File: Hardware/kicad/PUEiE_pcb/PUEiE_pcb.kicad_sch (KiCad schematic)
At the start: 7 parts, among them J1 Screw_Terminal_01x02, J3 USB_C_Receptacle_USB2.0_16P, U3 USBLC6-2SC6, U4 DRV8461SPWP, U6 LIS3MDL

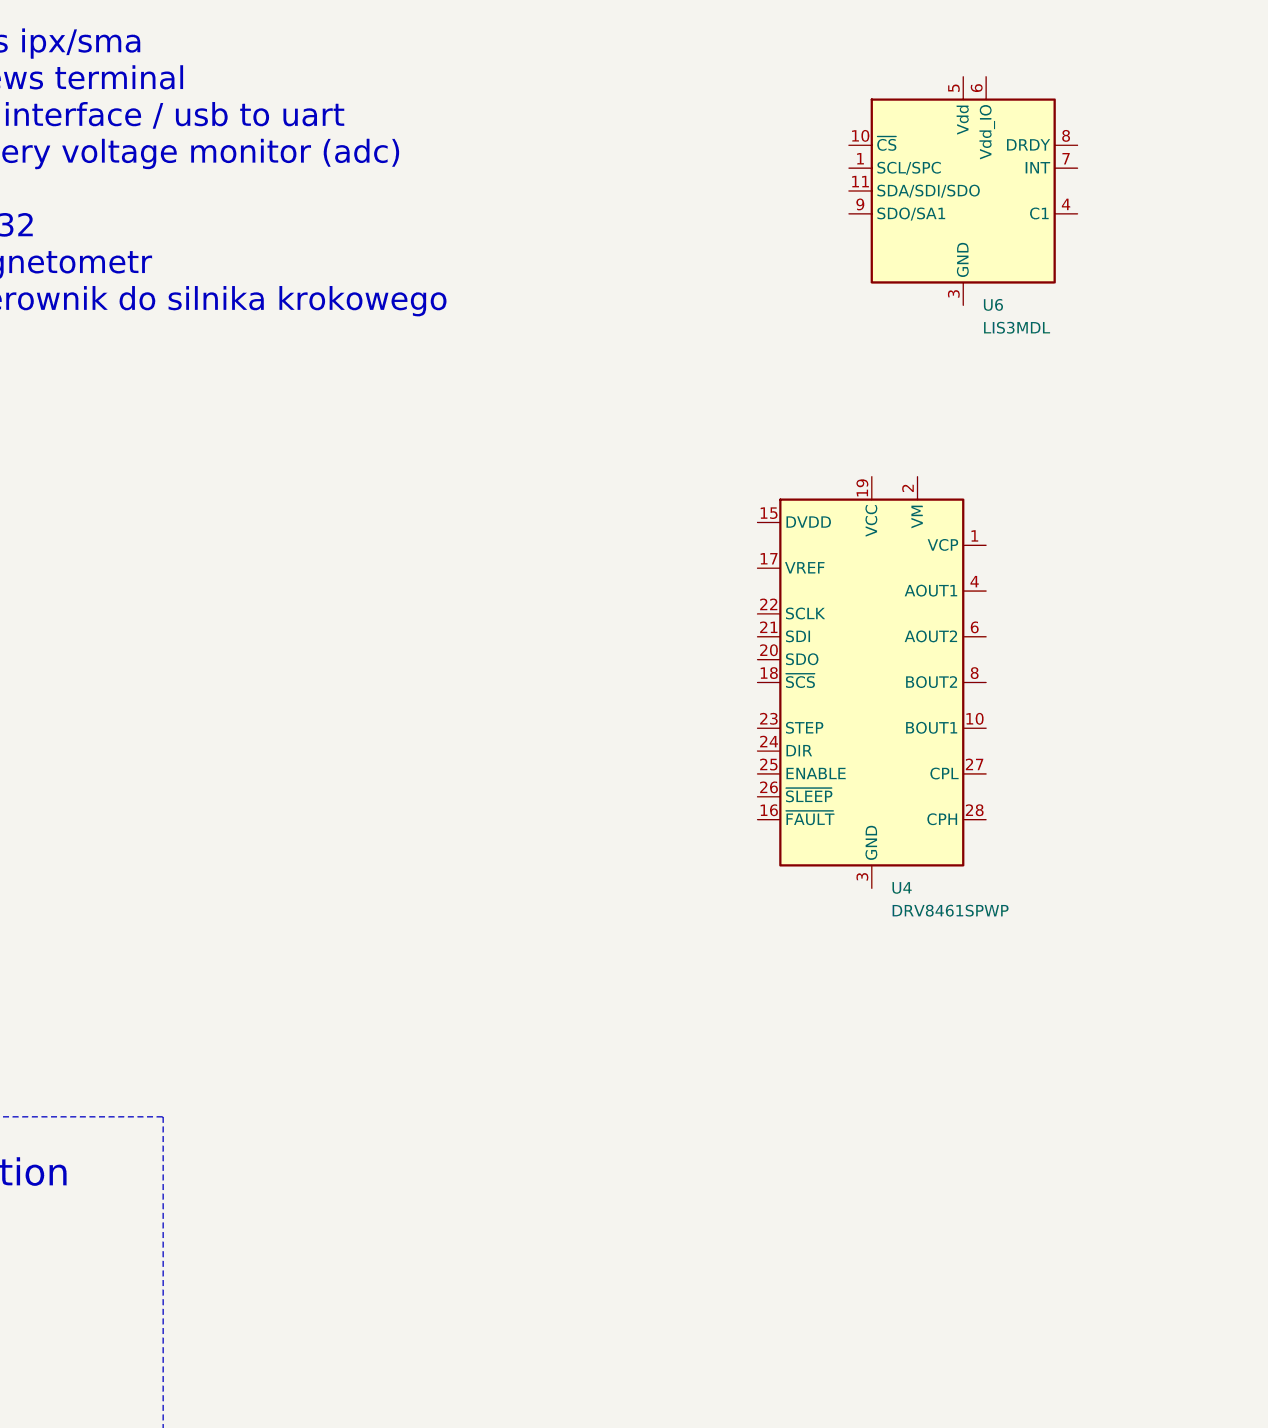
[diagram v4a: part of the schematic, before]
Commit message: magnetometer ,stepper controller
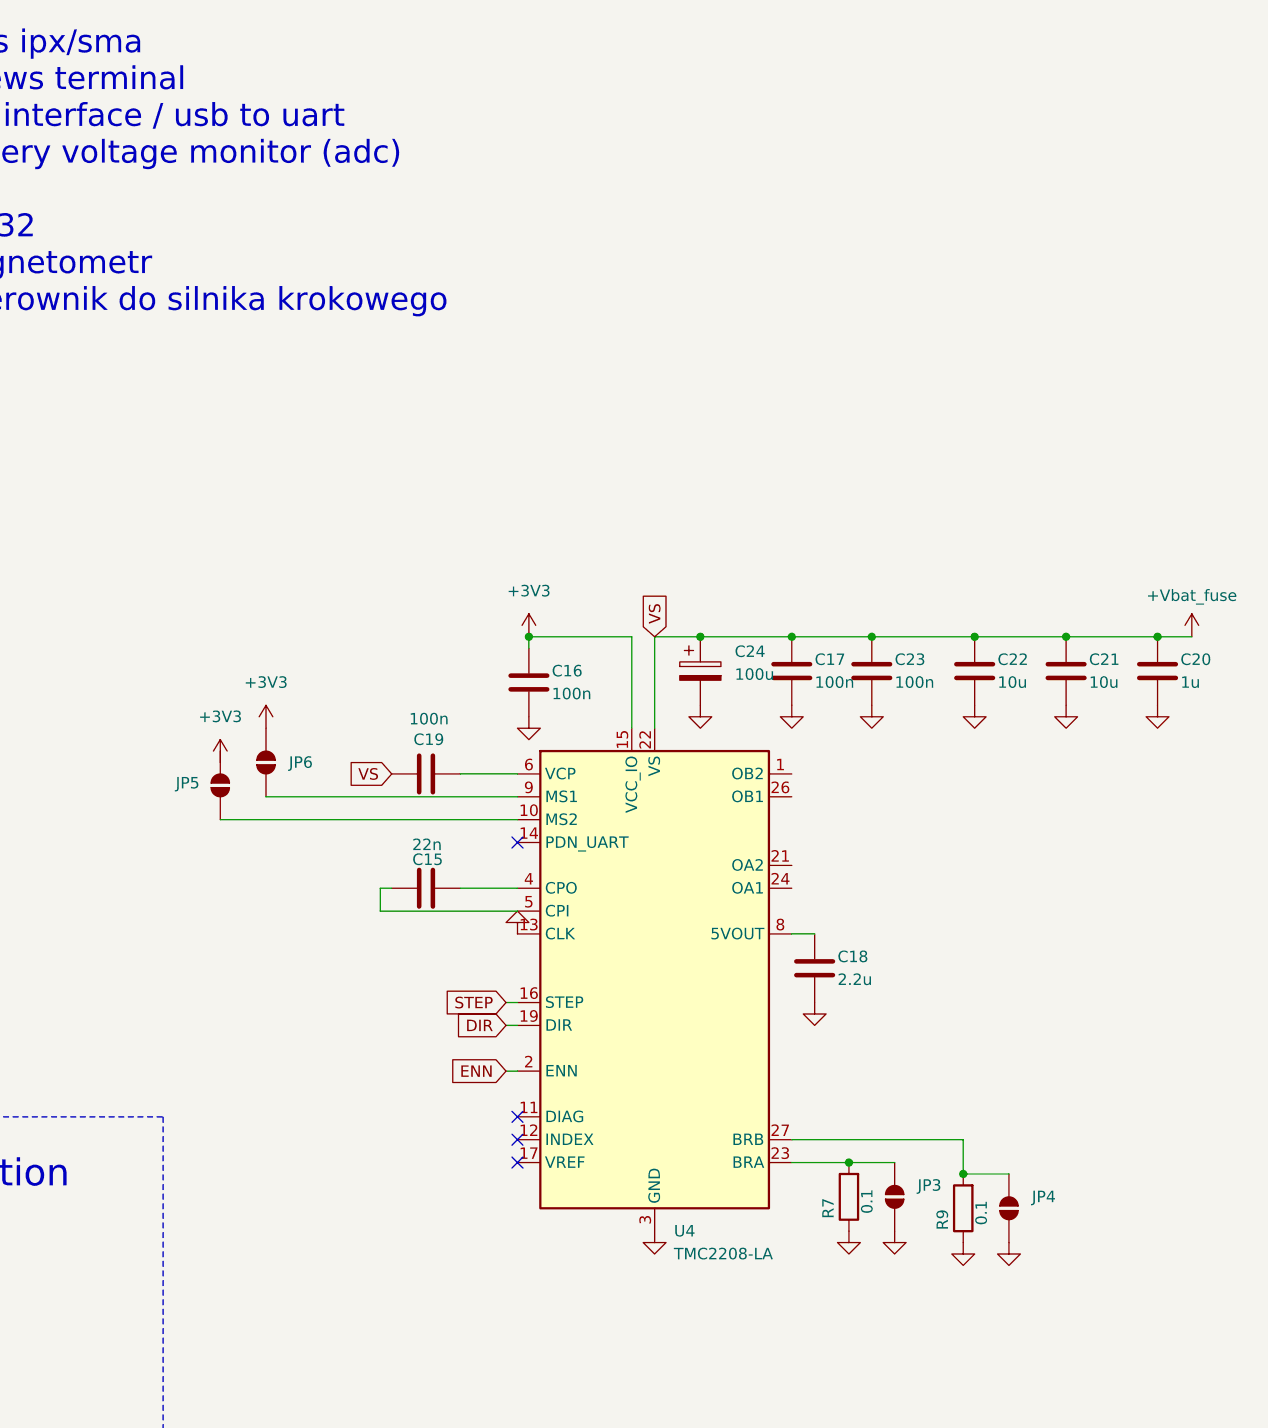
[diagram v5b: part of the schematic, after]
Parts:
- removed U4: DRV8461SPWP, Package_SO:Texas_PWP0020A, symbol Driver_Motor:DRV8461SPWP
- removed U6: LIS3MDL, Package_LGA:LGA-12_2x2mm_P0.5mm, symbol Sensor_Magnetic:LIS3MDL
- added C15: 22n, Capacitor_SMD:C_0805_2012Metric, symbol Device:C
- added C16, C17, C19, C23: 100n, Capacitor_SMD:C_0805_2012Metric, symbol Device:C
- added C18: 2.2u, Capacitor_SMD:C_0805_2012Metric, symbol Device:C
- added C20: 1u, Capacitor_SMD:C_0805_2012Metric, symbol Device:C
- added C21, C22: 10u, Capacitor_SMD:C_0805_2012Metric, symbol Device:C
- added C24: 100u, symbol Device:C_Polarized
- added JP3, JP4, JP5, JP6: SolderJumper_2_Open, symbol Jumper:SolderJumper_2_Open
- added R7, R9: 0.1, Resistor_SMD:R_1206_3216Metric, symbol Device:R
- added U4: TMC2208-LA, Package_DFN_QFN:TQFN-32-1EP_5x5mm_P0.5mm_EP3.4x3.4mm_ThermalVias, symbol Driver_Motor:TMC2208-LA
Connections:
- net GND: now also C16.2, C17.2, C18.2, C20.2, C21.2, C22.2, C23.2, C24.2, JP3.1 (A), JP4.1 (A), R7.1, R9.1, U4.13 (CLK), U4.18 (GND), U4.3 (GND)
- new net: JP3.2 (B), R7.2, U4.23 (BRA)
- new net: JP5.2 (B), U4.10 (MS2)
- new net: C19.2, U4.6 (VCP)
- new net: JP4.2 (B), R9.2, U4.27 (BRB)
- new net: C15.2, U4.4 (CPO)
- new net: C15.1, U4.5 (CPI)
- new net: C18.1, U4.8 (5VOUT)
- new net: JP6.2 (B), U4.9 (MS1)
- new net +3V3: C16.1, JP6.1 (A), U4.15 (VCC_IO)
- new net +Vbat_fuse: C17.1, C19.1, C20.1, C21.1, C22.1, C23.1, C24.1, U4.22 (VS), U4.28 (VS)
- new net DIR: U4.19 (DIR)
- new net ENN: U4.2 (ENN)
- new net STEP: U4.16 (STEP)
- no-connect marks 2 -> 6

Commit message: stm32WB55
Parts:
- removed C15: 22n, Capacitor_SMD:C_0805_2012Metric, symbol Device:C
- removed C16, C17, C19, C23: 100n, Capacitor_SMD:C_0805_2012Metric, symbol Device:C
- removed C18: 2.2u, Capacitor_SMD:C_0805_2012Metric, symbol Device:C
- removed C20: 1u, Capacitor_SMD:C_0805_2012Metric, symbol Device:C
- removed C21, C22: 10u, Capacitor_SMD:C_0805_2012Metric, symbol Device:C
- removed C24: 100u, symbol Device:C_Polarized
- removed JP3, JP4, JP5, JP6: SolderJumper_2_Open, symbol Jumper:SolderJumper_2_Open
- removed R7, R9: 0.1, Resistor_SMD:R_1206_3216Metric, symbol Device:R
- removed U4: TMC2208-LA, Package_DFN_QFN:TQFN-32-1EP_5x5mm_P0.5mm_EP3.4x3.4mm_ThermalVias, symbol Driver_Motor:TMC2208-LA
- added U7: STM32WB55CGU6, Package_DFN_QFN:QFN-48-1EP_7x7mm_P0.5mm_EP5.6x5.6mm, symbol MCU_ST_STM32WB:STM32WB55CGUx
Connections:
- net GND: now also U7.22 (VSSRF), U7.32 (VSSSMPS), U7.49 (VSS)
- no-connect marks 6 -> 2

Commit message: stm32WB
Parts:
- added C101, C105, C114: 4u7, Capacitor_SMD:C_0805_2012Metric, symbol Device:C
- added C102, C104, C106, C107, C108, C109, C110, C111, C112, C113: 100n, Capacitor_SMD:C_0805_2012Metric, symbol Device:C
- added C103: 100p, Capacitor_SMD:C_0805_2012Metric, symbol Device:C
- added C115: 0p8, Capacitor_SMD:C_0402_1005Metric, symbol Device:C
- added C116: 0p3, Capacitor_SMD:C_0402_1005Metric, symbol Device:C
- added C117, C118: c, Capacitor_SMD:C_0805_2012Metric, symbol Device:C
- added J103: ST-LINKv2, Connector_PinHeader_1.27mm:PinHeader_2x05_P1.27mm_Vertical, symbol STLINK-V3MINIE:STLINK-V3MINIE
- added J104: Conn_Coaxial, symbol Connector:Conn_Coaxial
- added L101: 10u, Inductor_SMD:L_0603_1608Metric, symbol Device:L
- added L102: 10n, Inductor_SMD:L_0402_1005Metric, symbol Device:L
- added L103: 2n7, Inductor_SMD:L_0402_1005Metric, symbol Device:L
- added R101: 0 ohm, Resistor_SMD:R_0805_2012Metric, symbol Device:R
- added R102: 220R, Resistor_SMD:R_0805_2012Metric, symbol Device:R
- added R103: 10k, Resistor_SMD:R_0201_0603Metric, symbol Device:R
- added SW101: SW_Push, symbol Switch:SW_Push
- added U102: DLF162500LT-5028A1, PUEiE_pcb_schematic_footprints:DLF162500LT-5028A1, symbol PUEiE_pcb_schematic_symbols:DLF162500LT-5028A1
- added Y101: 32MHz, symbol Device:Crystal_GND24
- added Y102: 32kHz768, symbol Device:Crystal
- R104: renamed from R4; footprint (none) -> Resistor_SMD:R_0805_2012Metric
- R105: renamed from R3; footprint (none) -> Resistor_SMD:R_0805_2012Metric
- renumbered J1 to J101, J3 to J102, U7 to U101, U3 to U103
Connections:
- net GND: now also C101.2, C102.2, C103.2, C104.2, C105.2, C106.2, C107.2, C108.2, C109.2, C110.2, C111.2, C112.2, C113.2, C114.2, C115.2, C116.2, C117.2, C118.2, J103.3 (T_JTMS/T_SWDIO), J103.8 (T_VCP_TX), J104.2 (Ext), R103.2, U102.2 (GND), U102.4 (GND), Y101.2, Y101.4
- net USB_D+: now also U101.38 (PA12)
- net USB_D-: now also U101.37 (PA11)
- net +3V3: now reaches U101.1 (VBAT)
- net +3V3: now also U101.20 (VDD), U101.23 (VDDRF), U101.34 (VDDSMPS), U101.35 (VDD), U101.40 (VDDUSB), U101.48 (VDD), U101.8 (VDDA), C101.1, C102.1, C103.1, C104.1, C105.1, C106.1, C107.1, C108.1, C109.1, C110.1, C111.1, R101.2, SW101.2
- net SPI_SCK: now reaches U101.10 (PA1)
- net SPI_MISO: now reaches U101.15 (PA6)
- net SPI_MOSI: now reaches U101.16 (PA7)
- net USART_RX: now reaches U101.18 (PA9)
- net USART_RX: now also U101.36 (PA10)
- net LSE_IN: now reaches U101.2 (PC14)
- net LSE_IN: now also C118.1, Y102.2
- net RF: now reaches U101.21 (RF1)
- net RF: now also C115.1, L103.1
- net HSE_OUT: now reaches U101.24 (OSC_OUT)
- net HSE_OUT: now also Y101.1
- net HSE_IN: now reaches U101.25 (OSC_IN)
- net HSE_IN: now also Y101.3
- net LSE_OUT: now reaches U101.3 (PC15)
- net LSE_OUT: now also C117.1, Y102.1
- net at U101.31 (VFBSMPS): now also C114.1, L102.2
- net at U101.33 (VLXSMPS): now also L101.1
- net SWDIO: now reaches U101.39 (PA13)
- net SWDIO: now also J103.9 (T_NRST)
- net BOOT0: now reaches U101.4 (PH3)
- net BOOT0: now also C112.1, R102.1, R103.1
- net SWCLK: now reaches U101.41 (PA14)
- net SWCLK: now also J103.10 (T_VCC)
- net PWM_MOTOR: now reaches U101.42 (PA15)
- net I2C_SCL: now reaches U101.5 (PB8)
- net I2C_SDA: now reaches U101.6 (PB9)
- net NRST: now reaches U101.7 (NRST)
- net NRST: now also C113.1, J103.1 (NC)
- net ADC_VBAT: now reaches U101.9 (PA0)
- new net: R102.2, SW101.1
- new net: L101.2, L102.1
- new net RF_ANT: J104.1 (In), U102.3 (OUT)
- new net RF_Matching_Network: C116.1, L103.2, U102.1 (IN)
- new net ST_linkv2_3V3: J103.4 (T_JCLK/T_SWCLK), J103.7 (T_VCP_RX), R101.1
- no-connect marks 2 -> 19
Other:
- sheet +3.3V Regulator ports: added Vbat_adc; removed none
- note added: "3.3V"
- note added: "5.0V"
- note added: "AN5165.pdf s14"
- note added: "BOOT0 Switch"
- note added: "GND"
- note added: "NRST"
- note added: "ST-LINKv2"
- note added: "SWCLK"
- note added: "SWDIO"
- note added: "SWIM"
- note added: "gnss ipx/sma screws terminal magnetometr sterownik do silnika krokowego"
- note removed: "gnss ipx/sma screws terminal usb interface / usb to uart battery voltage monitor (adc) stm32 magnetometr i sterownik do silnika krokowego"
- company: (none) -> Dominik Ledzianowski / Klaudia Lewandowska
- title: (none) -> Boat Autopilot Controller
- moved on the sheet: U101

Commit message: All Schematics
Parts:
- C101, C105, C114: Distributor (none) -> https://jlcpcb.com/partdetail/2131-CL21A475KAQNNNE/C1779; MFR Part (none) -> CL21A475KAQNNNE; Manufacturer (none) -> Samsung Electro-Mechanics
- C102, C104, C106, C107, C108, C109, C110, C111, C112, C113: Distributor (none) -> https://jlcpcb.com/partdetail/28983-CL21B104KCFNNNE/C28233; MFR Part (none) -> CL21B104KCFNNNE; Manufacturer (none) -> Samsung Electro-Mechanics
- C103: Distributor (none) -> https://jlcpcb.com/partdetail/2142-CL21C101JBANNNC/C1790; MFR Part (none) -> CL21C101JBANNNC; Manufacturer (none) -> Samsung Electro-Mechanics
- C115: Distributor (none) -> https://jlcpcb.com/partdetail/MurataElectronics-GRM1555C1HR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; MFR Part (none) -> GRM1555C1HR80BA01D; Manufacturer (none) -> Murata Electronics
- C116: Distributor (none) -> https://jlcpcb.com/partdetail/MurataElectronics-GRM1555C1HR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; MFR Part (none) -> GRM1555C1HR30WA01D; Manufacturer (none) -> Murata Electronics
- C117, C118: value c -> 10p; footprint Capacitor_SMD:C_0805_2012Metric -> Capacitor_SMD:C_0603_1608Metric; Distributor (none) -> https://jlcpcb.com/partdetail/1986-CL10C100JB8NNNC/C1634; MFR Part (none) -> CL10C100JB8NNNC; Manufacturer (none) -> Samsung Electro-Mechanics
- J101: footprint (none) -> TerminalBlock_Phoenix:TerminalBlock_Phoenix_PT-1,5-2-3.5-H_1x02_P3.50mm_Horizontal; Distributor (none) -> https://www.mouser.pl/ProductDetail/SparkFun/PRT-08084?qs=W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; MFR Part (none) -> PRT-08084; Manufacturer (none) -> SparkFun
- J102: Distributor (none) -> https://jlcpcb.com/partdetail/3554049-USB4105_GF_A060/C3025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; Link 1 https://jlcpcb.com/partdetail/3554049-USB4105_GF_A060/C3025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 -> (none); MFR Part (none) -> USB4105-GF-A-060; Manufacturer (none) -> Global Connector Technology
- J103: Distributor (none) -> https://jlcpcb.com/partdetail/hanxia-HX_JN1_27_2x5P_ZZ_H49/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; MFR Part (none) -> HX JN1.27-2x5P ZZ H4.9; Manufacturer (none) -> hanxia
- J104: value Conn_Coaxial -> Conn_IPEX; footprint (none) -> PUEiE_pcb_schematic_footprints:IPEX Male; Distributor (none) -> https://jlcpcb.com/partdetail/BATWIRELESS-BWIPX_1001E/C4965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; MFR Part (none) -> BWIPX-1-001E; Manufacturer (none) -> BAT WIRELESS
- L101: Distributor (none) -> https://jlcpcb.com/partdetail/Sunlord-SDFL1608S100KTF/C1035; MFR Part (none) -> SDFL1608S100KTF; Manufacturer (none) -> Sunlord
- L102: Distributor (none) -> https://jlcpcb.com/partdetail/MurataElectronics-LQG15WZ10NJ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; MFR Part (none) -> LQG15WZ10NJ02D; Manufacturer (none) -> Murata Electronics
- L103: Distributor (none) -> https://jlcpcb.com/partdetail/MurataElectronics-LQG15HS2N7S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; MFR Part (none) -> LQG15HS2N7S02D; Manufacturer (none) -> Murata Electronics
- R101: Distributor (none) -> https://jlcpcb.com/partdetail/18165-0805W8F0000T5E/C17477; JLCPCB Part #  C17477 -> (none); MFR Part (none) -> 0805W8F0000T5E; MFR.Part # 0805W8F0000T5E -> (none); Manufacturer (none) -> UNI-ROYAL(Uniroyal Elec)
- R102: Distributor (none) -> https://jlcpcb.com/partdetail/18245-0805W8F2200T5E/C17557; MFR Part (none) -> 0805W8F2200T5E; Manufacturer (none) -> UNI-ROYAL(Uniroyal Elec)
- R103: footprint Resistor_SMD:R_0201_0603Metric -> Resistor_SMD:R_0805_2012Metric; Distributor (none) -> https://jlcpcb.com/partdetail/18102-0805W8F1002T5E/C17414; MFR Part (none) -> 0805W8F1002T5E; Manufacturer (none) -> UNI-ROYAL(Uniroyal Elec)
- R104, R105: Distributor (none) -> https://jlcpcb.com/partdetail/28584-0805W8F5101T5E/C27834; MFR Part (none) -> 0805W8F5101T5E; Manufacturer (none) -> UNI-ROYAL(Uniroyal Elec)
- SW101: footprint (none) -> PUEiE_pcb_schematic_footprints:SW_2pin_5.5x2.0mm; Distributor (none) -> https://jlcpcb.com/partdetail/XUNPU-TS_1088AR02016/C720477; MFR Part (none) -> TS-1088-AR02016; Manufacturer (none) -> XUNPU
- U101: Distributor (none) -> https://jlcpcb.com/partdetail/STMicroelectronics-STM32WB55C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; Link 1 https://jlcpcb.com/partdetail/STMicroelectronics-STM32WB55C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 -> (none); MFR Part (none) -> STM32WB55CGU6; Manufacturer (none) -> STMicroelectronics
- U102: Distributor (none) -> https://jlcpcb.com/partdetail/TDK-DLF162500LT5028A1/C531364; MFR Part (none) -> DLF162500LT-5028A1; Manufacturer (none) -> TDK
- U103: Distributor (none) -> https://jlcpcb.com/partdetail/STMicroelectronics-USBLC62SC6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; Likn 1 https://jlcpcb.com/partdetail/STMicroelectronics-USBLC62SC6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 -> (none); MFR Part (none) -> USBLC6-2SC6; Manufacturer (none) -> STMicroelectronics
- Y101: footprint (none) -> Crystal:Crystal_SMD_2016-4Pin_2.0x1.6mm; Distributor (none) -> https://jlcpcb.com/partdetail/NDK-NX2016SA_32MHZ_STD_CZS5/C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; MFR Part (none) -> NX2016SA-32MHZ-STD-CZS-5; Manufacturer (none) -> NDK
- Y102: footprint (none) -> Crystal:Crystal_SMD_2012-2Pin_2.0x1.2mm; Distributor (none) -> https://jlcpcb.com/partdetail/NDK-NX2012SA_32_768KHZ_STD_MU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; MFR Part (none) -> NX2012SA 32.768KHZ STD-MUB-1; Manufacturer (none) -> NDK
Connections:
- net USART_RX: no longer U101.36 (PA10)
- net BOOT0_SW: now reaches R102.2, SW101.1
- net VLXSMPS: now reaches L101.1, U101.33 (VLXSMPS)
- net VLXSMPS_L: now reaches L101.2, L102.1
- net VFBSMPS: now reaches C114.1, L102.2, U101.31 (VFBSMPS)
- net ~{GPS_RESET}: now reaches U101.19 (PB2)
- net MOTOR_DIR: now reaches U101.43 (PB3)
- net MAG_~{CS}: now reaches U101.44 (PB4)
- net SMD_STEP: now reaches U101.45 (PB5)
- net SMD_DIR: now reaches U101.46 (PB6)
- net SMD_ENN: now reaches U101.47 (PB7)
- net PWM_MOTOR renamed MOTOR_PWM
- new net USART_TX: U101.36 (PA10)
- no-connect marks 19 -> 13
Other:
- sheet Interfaces ports: added I2C_SCL, I2C_SDA, MAG_~{CS}, MOTOR_DIR, MOTOR_PWM, SMD_DIR, SMD_ENN, SMD_STEP, SPI_MISO, SPI_MOSI, SPI_SCK, USART_RX, USART_TX, ~{GPS_RESET}; removed none
- note removed: "12V 46lbs -> MAX 40 AMP 50 AMP FUSE 10.5V - 15.0V"
- note removed: "gnss ipx/sma screws terminal magnetometr sterownik do silnika krokowego"
- moved on the sheet: C103, C104, C112, C113, L101, R102, SW101
